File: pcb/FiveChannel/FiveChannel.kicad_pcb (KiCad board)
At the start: 2 copper layers, 47 x 31.4 mm, 211 parts, among them J101 UPDI, J102 5V In, J103 Conn_01x04_Male, J104 Conn_01x07_Male, J201 Conn_01x20_Male, U101 74LS596, U102 ATTINY1614

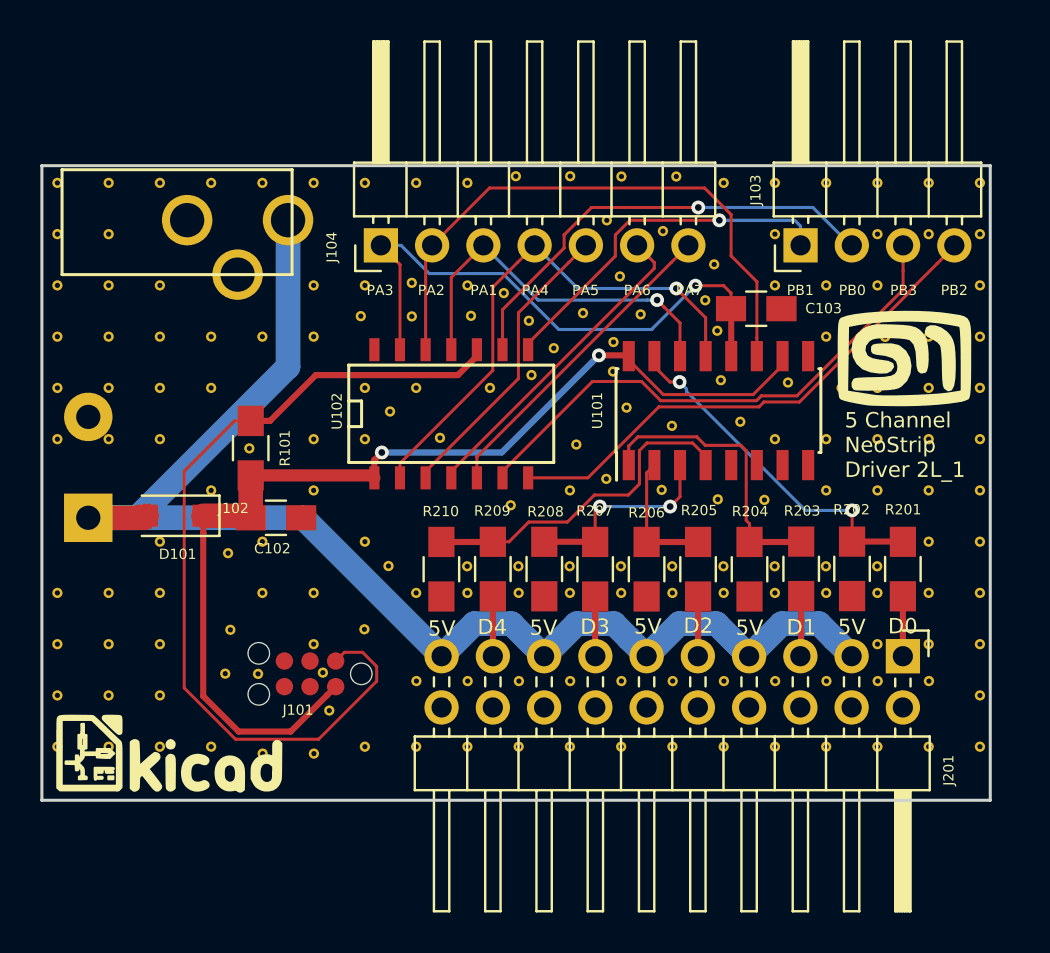
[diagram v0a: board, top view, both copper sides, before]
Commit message: Finished 8Channel and submitted to Fab
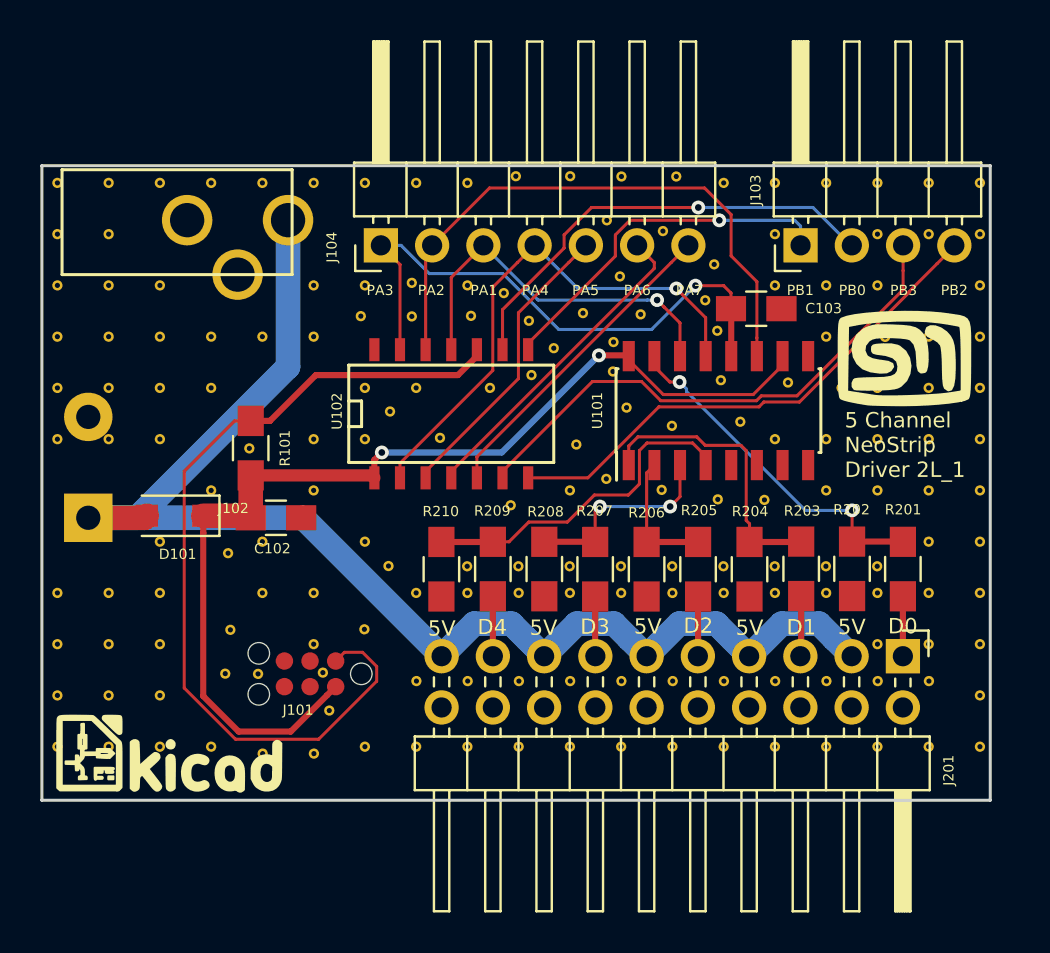
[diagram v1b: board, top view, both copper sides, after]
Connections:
- net /~ENABLE renamed /~{ENABLE}
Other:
- net class Default removed

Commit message: Hard merge of 5 channel restore (#4)
Co-authored-by: Steve Mayze <smayze@yahoo.com##>
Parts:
- removed G***: LOGO, advent_sternla:KiCad-Logo
- removed G*** (x2): LOGO, advent_sternla:MyBasic_rounded_50_1
- removed REF***: KiCad-Logo2_6mm_SilkScreen, Symbols:KiCad-Logo2_6mm_SilkScreen
- removed ST** (x185): STITCH_VIA, advent_sternla:STITCH_VIA
- U101: value 74LS596 -> 74LS595
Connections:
- J101 pad 3: (no net) -> unconnected-(J101-Pin_3-Pad3)
- J101 pad 4: (no net) -> unconnected-(J101-Pin_4-Pad4)
- J101 pad 5: (no net) -> unconnected-(J101-Pin_5-Pad5)
- J102 pad 3: (no net) -> unconnected-(J102-Pad3)
- U101 pad 5: (no net) -> unconnected-(U101-QF-Pad5)
- U101 pad 6: (no net) -> unconnected-(U101-QG-Pad6)
- U101 pad 7: (no net) -> unconnected-(U101-QH-Pad7)
- U101 pad 9: (no net) -> unconnected-(U101-~{QH}-Pad9)
